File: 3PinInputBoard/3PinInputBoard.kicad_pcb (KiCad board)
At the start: 2 copper layers, 50.8 x 25.4 mm, 19 parts, among them J1 ICSP, J2 POWER/CAN, J3 Conn_01x04, J4 Conn_01x03, U1 ATtiny841-SS, U2 MCP25625-x-SS, U3 74HC04

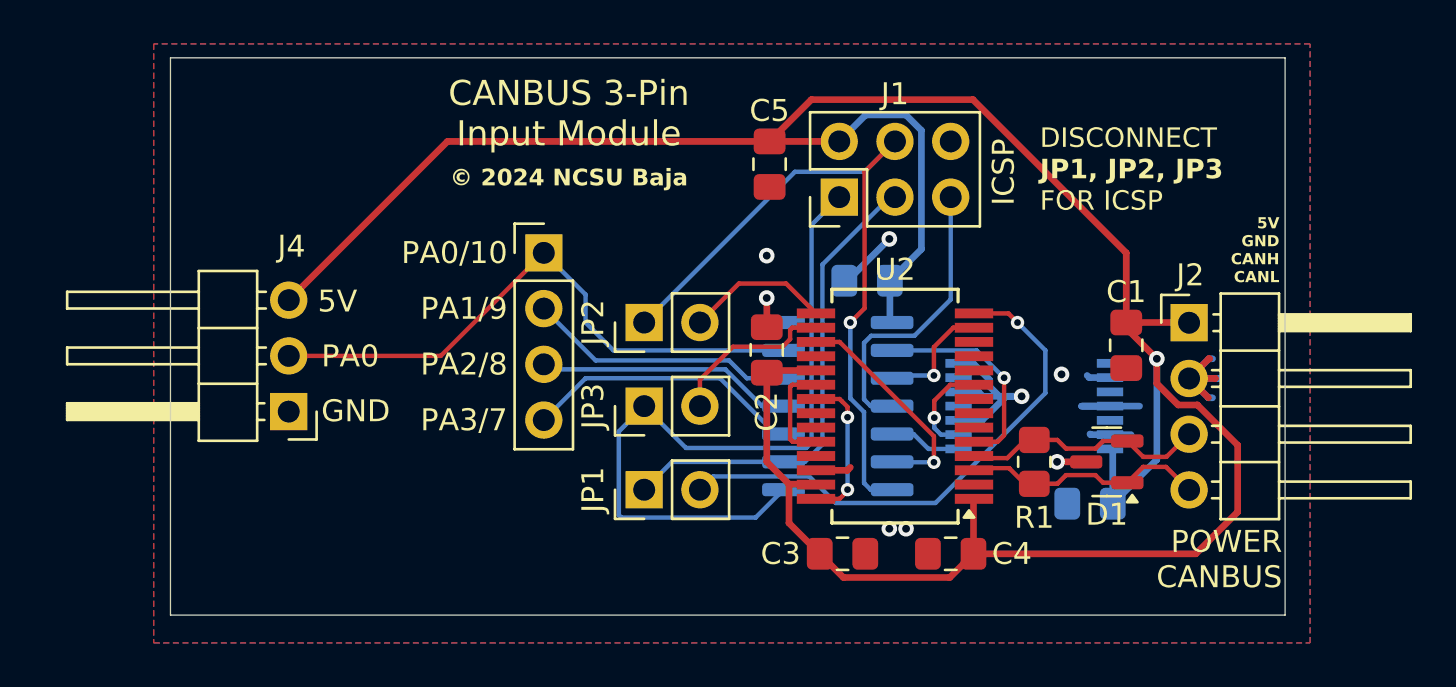
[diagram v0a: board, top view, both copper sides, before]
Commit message: Fixed sensor input header
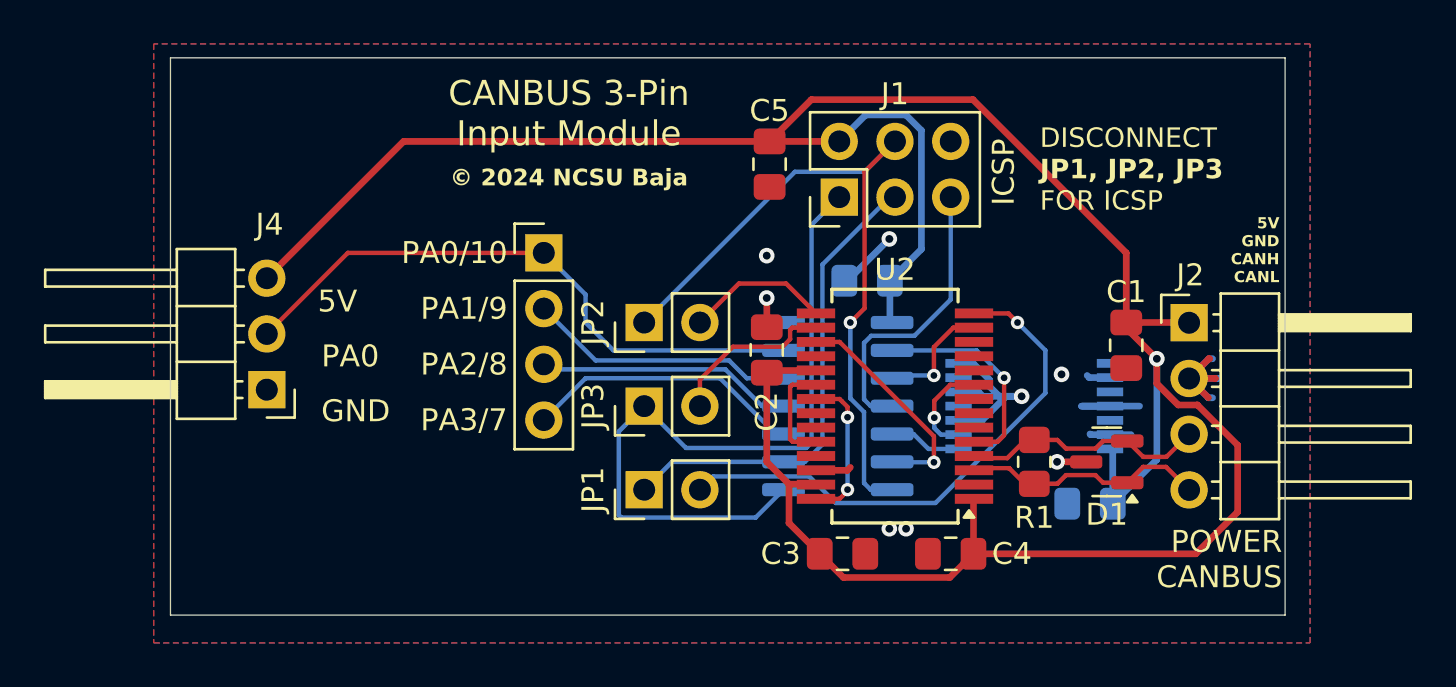
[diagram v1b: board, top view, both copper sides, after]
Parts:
- moved J4 1.41 mm to (114.4, 104.0)
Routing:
- net /USER0: track 27.1 -> 27.7 mm
- net +5V: track 125.3 -> 125.8 mm
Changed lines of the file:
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@@
 	(footprint "Connector_PinHeader_2.54mm:PinHeader_1x03_P2.54mm_Horizontal"
 		(layer "F.Cu")
-		(at 115.375 105.025 180)
+		(at 114.375 104.025 180)
 		(descr "Through hole angled pin header, 1x03, 2.54mm pitch, 6mm pin length, single row")
 		(tags "Through hole angled pin header THT 1x03 2.54mm single row")
 		(property "Reference" "J4"
-			(at -0.125 7.525 360)
+			(at -0.125 7.525 0)
 			(layer "F.SilkS")
 			(effects
@@
 		)
 		(property "Value" "Conn_01x03"
-			(at 4.385 7.35 360)
+			(at 4.385 7.35 0)
 			(layer "F.Fab")
 			(effects
@@
 	)
 	(segment
-		(start 115.375 99.945)
-		(end 122.61 92.71)
+		(start 114.375 98.945)
+		(end 120.61 92.71)
 		(width 0.3048)
 		(layer "F.Cu")
@@
 	)
 	(segment
-		(start 122.61 92.71)
-		(end 137.29 92.71)
-		(width 0.3048)
-		(layer "F.Cu")
-		(net 2)
-	)
-	(segment
 		(start 158.623 109.601)
 		(end 158.623 106.553)
@@
 	)
 	(segment
+		(start 120.61 92.71)
+		(end 137.29 92.71)
+		(width 0.3048)
+		(layer "F.Cu")
+		(net 2)
+	)
+	(segment
 		(start 153.546 100.965)
 		(end 153.546 101.222)
@@
 	)
 	(segment
-		(start 122.305 102.485)
-		(end 127 97.79)
+		(start 118.07 97.79)
+		(end 114.375 101.485)
 		(width 0.2032)
 		(layer "F.Cu")
@@
 	)
 	(segment
-		(start 115.375 102.485)
-		(end 122.305 102.485)
+		(start 127 97.79)
+		(end 118.07 97.79)
 		(width 0.2032)
 		(layer "F.Cu")

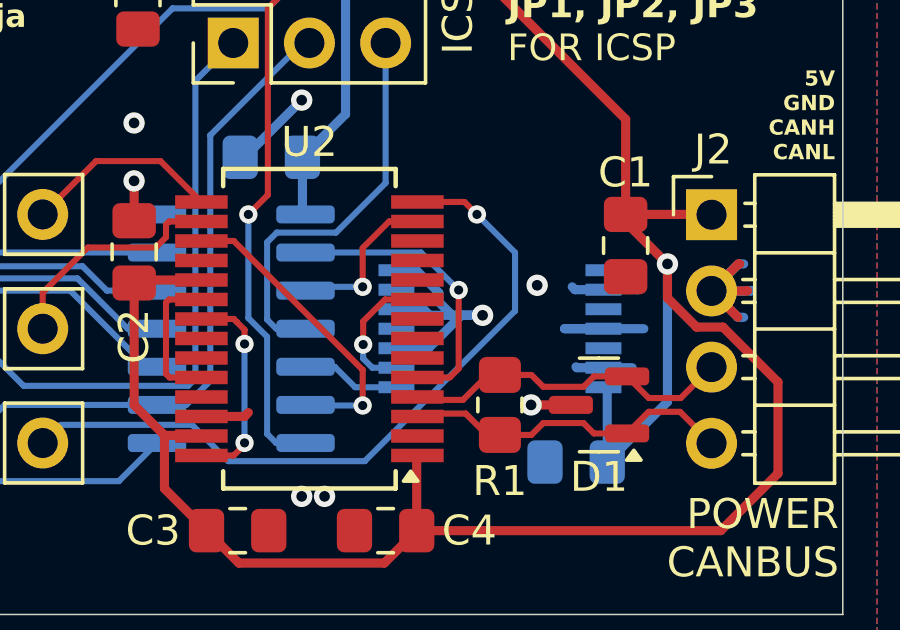
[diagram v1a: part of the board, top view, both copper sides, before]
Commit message: Fixed grounds
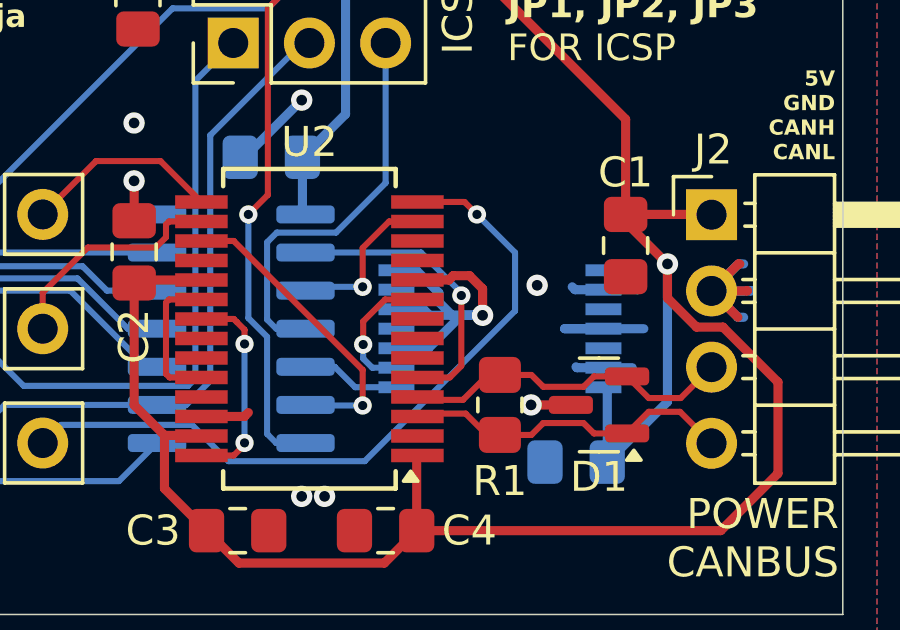
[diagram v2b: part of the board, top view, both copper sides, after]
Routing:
- net GND: track 33.2 -> 36.5 mm
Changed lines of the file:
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@@
+	)
+	(segment
+		(start 146.605 103.15)
+		(end 147.65272 103.15)
+		(width 0.3048)
+		(layer "F.Cu")
+		(net 1)
+	)
+	(segment
+		(start 147.65272 103.15)
+		(end 147.795693 103.007027)
+		(width 0.3048)
+		(layer "F.Cu")
+		(net 1)
+	)
+	(segment
+		(start 148.342787 103.007027)
+		(end 148.777826 103.442066)
+		(width 0.3048)
+		(layer "F.Cu")
+		(net 1)
+	)
+	(segment
+		(start 147.795693 103.007027)
+		(end 148.342787 103.007027)
+		(width 0.3048)
+		(layer "F.Cu")
+		(net 1)
 	)
 	(segment
 		(start 156.41 103.515)
 		(end 157.309 102.616)
+		(width 0.3048)
+		(layer "F.Cu")
+		(net 1)
+	)
+	(segment
+		(start 148.777826 103.442066)
+		(end 148.777826 104.327826)
 		(width 0.3048)
 		(layer "F.Cu")
@@
 	)
 	(segment
-		(start 147.979911 103.484701)
-		(end 147.979911 106.103289)
+		(start 148.06924 106.01396)
+		(end 147.6832 106.4)
 		(width 0.2032)
 		(layer "F.Cu")
@@
 	)
 	(segment
-		(start 147.979911 106.103289)
-		(end 147.6832 106.4)
+		(start 148.06924 103.667427)
+		(end 148.06924 106.01396)
 		(width 0.2032)
 		(layer "F.Cu")
@@
 	)
 	(via
-		(at 147.979911 103.484701)
+		(at 148.06924 103.667427)
 		(size 0.6096)
 		(drill 0.3048)
@@
 	)
 	(segment
-		(start 147.979911 103.484701)
-		(end 147.974301 103.484701)
-		(width 0.2032)
-		(layer "B.Cu")
-		(net 12)
-	)
-	(segment
 		(start 146.7246 102.235)
 		(end 142.875 102.235)
@@
 	)
 	(segment
-		(start 147.974301 103.484701)
+		(start 148.06924 103.667427)
+		(end 148.06924 103.57964)
+		(width 0.2032)
+		(layer "B.Cu")
+		(net 12)
+	)
+	(segment
+		(start 148.06924 103.57964)
 		(end 146.7246 102.235)
 		(width 0.2032)
